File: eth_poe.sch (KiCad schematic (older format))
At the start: 43 parts, among them J201 HR861153C, U201 W5500, Y201 25MHz

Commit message: Prep for gerber export
Update fields
Align standoff holes
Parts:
- U201: Manufacturer (none) -> WIZnet
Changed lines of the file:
@@
 F 6 "W5500" H 7100 3100 50  0001 C CNN "MPN"
 F 7 "C32843" H 7100 3100 50  0001 C CNN "LCSC"
+F 8 "WIZnet" H 7100 3100 50  0001 C CNN "Manufacturer"
 	1    7100 3100
 	1    0    0    -1

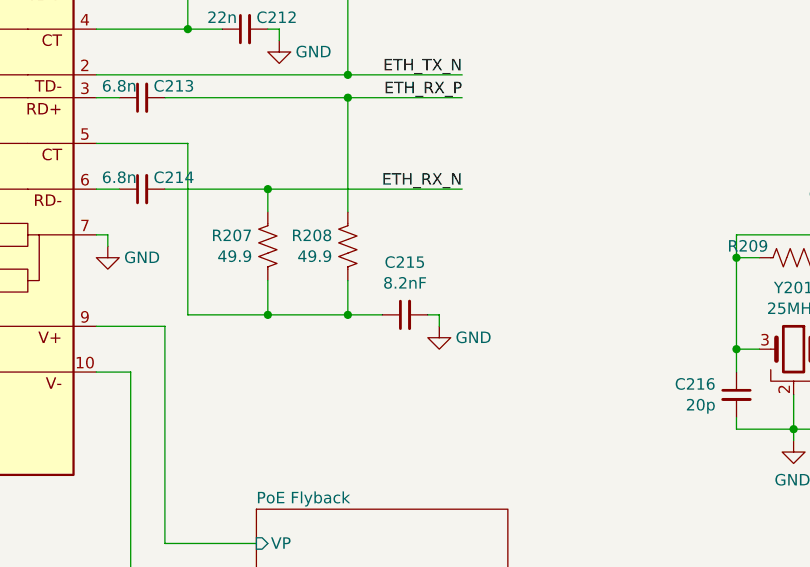
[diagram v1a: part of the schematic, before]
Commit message: Schematic field cleanup
Remove stray spaces
Cleaned up duplicate fields
Normalize: 100pF (C314 C803 C807) and 47uF  (C308 C310 C804 C805) according to r0 order
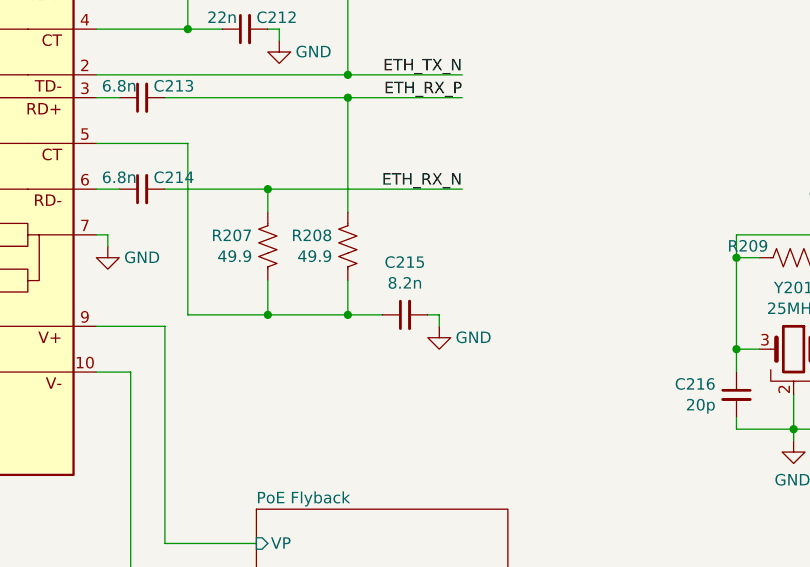
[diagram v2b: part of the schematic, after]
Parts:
- C215: value 8.2nF -> 8.2n; Alt CAP CER 6800PF 50V X7R 0603 -> (none); Current CAP CER 6800PF 50V X7R 0603 -> (none); Description CAP CER 6800PF 50V X7R 0603 -> (none); Error CAP CER 6800PF 50V X7R 0603 -> (none); Mfr CAP CER 6800PF 50V X7R 0603 -> (none); Size (none) -> 0603; Type (none) -> X7R; Voltage (none) -> 50V
- FB201: Alt Ferrite_Bead_Small -> (none); Current Ferrite_Bead_Small -> (none); Description Ferrite_Bead_Small -> (none); Error Ferrite_Bead_Small -> (none); Mfr 470 Ohms @ 100MHz 1 Power Line Ferrite Bead 0603 1A 200mOhm -> (none); Mouser 81-BLM18PG471SN1D -> (none)
- R201: LCSC C109317 -> C109317
- Y201: LCSC C91738, C255955 -> C91738, C255955; MPN X1E000021035200 -> X1E000021035200
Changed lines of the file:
@@
 AR Path="/5FCEDB09/5FAC68EB" Ref="C215"  Part="1"
 F 0 "C215" V 3521 3550 50  0000 C CNN
-F 1 "8.2nF" V 3612 3550 50  0000 C CNN
+F 1 "8.2n" V 3612 3550 50  0000 C CNN
 F 2 "Capacitor_SMD:C_0603_1608Metric" H 3750 3550 50  0001 C CNN
-F 3 "CAP CER 6800PF 50V X7R 0603" H 3750 3550 50  0001 C CNN
-F 4 "CAP CER 6800PF 50V X7R 0603" H 3750 3550 50  0001 C CNN "Alt"
-F 5 "CAP CER 6800PF 50V X7R 0603" H 3750 3550 50  0001 C CNN "Current"
-F 6 "CAP CER 6800PF 50V X7R 0603" H 3750 3550 50  0001 C CNN "Description"
-F 7 "311-1811-1-ND" H 3750 3550 50  0001 C CNN "Digikey"
-F 8 "CAP CER 6800PF 50V X7R 0603" H 3750 3550 50  0001 C CNN "Error"
-F 9 "C113812" H 3750 3550 50  0001 C CNN "LCSC"
-F 10 "CC0603KRX7R9BB822" H 3750 3550 50  0001 C CNN "MPN"
-F 11 "CAP CER 6800PF 50V X7R 0603" H 3750 3550 50  0001 C CNN "Mfr"
-F 12 "CAP CER 8.2NF X7R 50V 0603" H 3750 3550 50  0001 C CNN "Note"
+F 3 "" H 3750 3550 50  0001 C CNN
+F 4 "311-1811-1-ND" H 3750 3550 50  0001 C CNN "Digikey"
+F 5 "" H 3750 3550 50  0001 C CNN "Error"
+F 6 "C113812" H 3750 3550 50  0001 C CNN "LCSC"
+F 7 "CC0603KRX7R9BB822" H 3750 3550 50  0001 C CNN "MPN"
+F 8 "" H 3750 3550 50  0001 C CNN "Mfr"
+F 9 "CAP CER 8.2NF X7R 50V 0603" H 3750 3550 50  0001 C CNN "Note"
+F 10 "0603" H 3750 3550 50  0001 C CNN "Size"
+F 11 "X7R" H 3750 3550 50  0001 C CNN "Type"
+F 12 "50V" H 3750 3550 50  0001 C CNN "Voltage"
 	1    3750 3550
 	0    -1   1    0
@@
 F 5 "311-10GRDKR-ND" H 2800 1400 50  0001 C CNN "Digikey"
 F 6 "RES SMD 10 OHM 5% 1/10W 0603" H 2800 1400 50  0001 C CNN "Note"
-F 7 " C109317 " H 2800 1400 50  0001 C CNN "LCSC"
+F 7 "C109317" H 2800 1400 50  0001 C CNN "LCSC"
 	1    2800 1400
 	1    0    0    1
@@
 F 1 "Ferrite_Bead_Small" V 6954 1250 50  0001 C CNN
 F 2 "Inductor_SMD:L_0603_1608Metric" V 7030 1250 50  0001 C CNN
-F 3 "Ferrite_Bead_Small" H 7100 1250 50  0001 C CNN
-F 4 "Ferrite_Bead_Small" H 7100 1250 50  0001 C CNN "Alt"
-F 5 "490-5223-1-ND" H 7100 1250 50  0001 C CNN "Digikey"
-F 6 "Ferrite_Bead_Small" H 7100 1250 50  0001 C CNN "Error"
-F 7 "C97853" H 7100 1250 50  0001 C CNN "LCSC"
-F 8 "BLM18PG471SN1D" H 7100 1250 50  0001 C CNN "MPN"
-F 9 "" H 7100 1250 50  0001 C CNN "Manufacturer"
-F 10 "470 Ohms @ 100MHz 1 Power Line Ferrite Bead 0603 1A 200mOhm" H 7100 1250 50  0001 C CNN "Mfr"
-F 11 "470 Ohms @ 100MHz 1 Power Line Ferrite Bead 0603 1A 200mOhm" H 7100 1250 50  0001 C CNN "Note"
-F 12 "Ferrite_Bead_Small" H 7100 1250 50  0001 C CNN "Current"
-F 13 "Ferrite_Bead_Small" H 7100 1250 50  0001 C CNN "Description"
-F 14 "81-BLM18PG471SN1D " H 7100 1250 50  0001 C CNN "Mouser"
+F 3 "" H 7100 1250 50  0001 C CNN
+F 4 "490-5223-1-ND" H 7100 1250 50  0001 C CNN "Digikey"
+F 5 "C97853" H 7100 1250 50  0001 C CNN "LCSC"
+F 6 "BLM18PG471SN1D" H 7100 1250 50  0001 C CNN "MPN"
+F 7 "470 Ohms @ 100MHz 1 Power Line Ferrite Bead 0603 1A 200mOhm" H 7100 1250 50  0001 C CNN "Note"
 	1    7100 1250
 	0    1    1    0
@@
 F 2 "Crystal:Crystal_SMD_3225-4Pin_3.2x2.5mm" H 5450 3700 50  0001 C CNN
 F 3 "~" H 5450 3700 50  0001 C CNN
-F 4 "X1E000021035200 " H 5450 3700 50  0001 C CNN "MPN"
+F 4 "X1E000021035200" H 5450 3700 50  0001 C CNN "MPN"
 F 5 "SER4375CT-ND" H 5450 3700 50  0001 C CNN "Digikey"
 F 6 "CRYSTAL 25MHZ 20PF SMD" H 5450 3700 50  0001 C CNN "Note"
-F 7 " C91738, C255955" H 5450 3700 50  0001 C CNN "LCSC"
+F 7 "C91738, C255955" H 5450 3700 50  0001 C CNN "LCSC"
 	1    5450 3700
 	-1   0    0    -1
